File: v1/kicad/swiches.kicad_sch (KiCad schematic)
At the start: 13 parts, among them Q7 BC337

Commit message: Changed the file structure
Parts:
- SW1: value (none) -> SPST
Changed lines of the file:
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@@
 			)
 		)
-		(property "Value" ""
+		(property "Value" "SPST"
 			(at 64.77 55.88 0)
+			(hide yes)
 			(show_name no)
 			(do_not_autoplace no)
@@
 			)
 		)
-		(property "Description" "NPN transistor, collector/base/emitter"
+		(property "Description" ""
 			(at 88.9 55.88 0)
 			(hide yes)
@@
 			)
 		)
-		(property "Description" "Light emitting diode"
+		(property "Description" ""
 			(at 135.89 48.26 0)
 			(hide yes)
@@
 			)
 		)
-		(property "Description" "100V 0.15A standard switching diode, DO-35"
+		(property "Description" ""
 			(at 88.9 39.37 0)
 			(hide yes)
@@
 			)
 		)
-		(property "Description" "100V 0.15A standard switching diode, DO-35"
+		(property "Description" ""
 			(at 105.41 39.37 0)
 			(hide yes)
@@
 			)
 		)
-		(property "Description" "100V 0.15A standard switching diode, DO-35"
+		(property "Description" ""
 			(at 123.19 39.37 0)
 			(hide yes)
@@
 			)
 		)
-		(property "Description" "Light emitting diode"
+		(property "Description" ""
 			(at 140.97 48.26 0)
 			(hide yes)

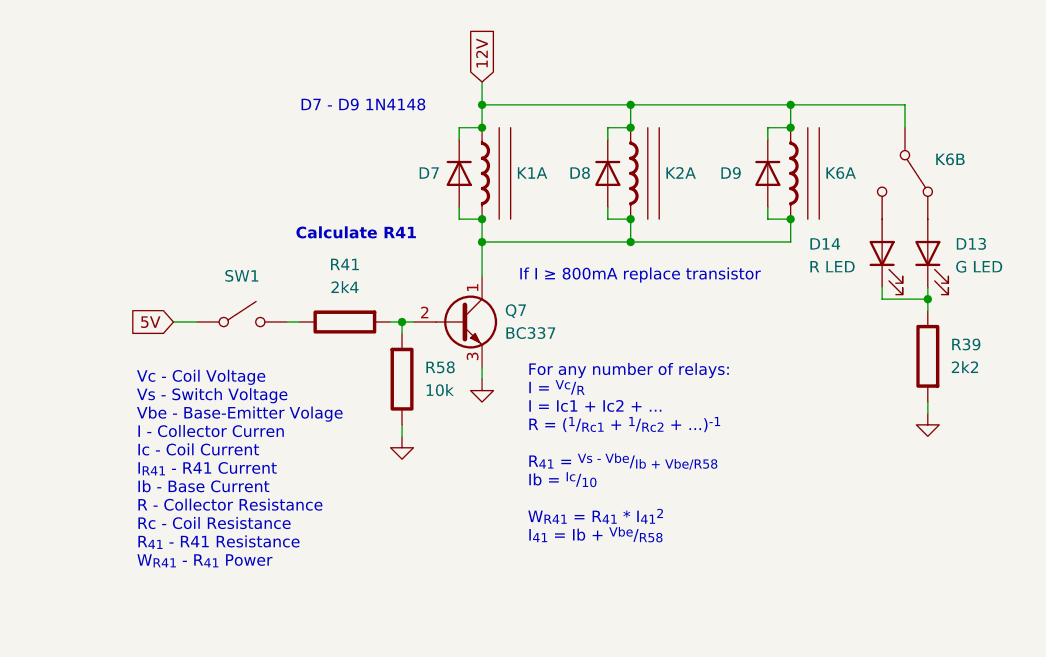
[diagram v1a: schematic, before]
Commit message: Added a DUT board, changed the output connectors , added test hooks, removed unnecessary switches, added FET support
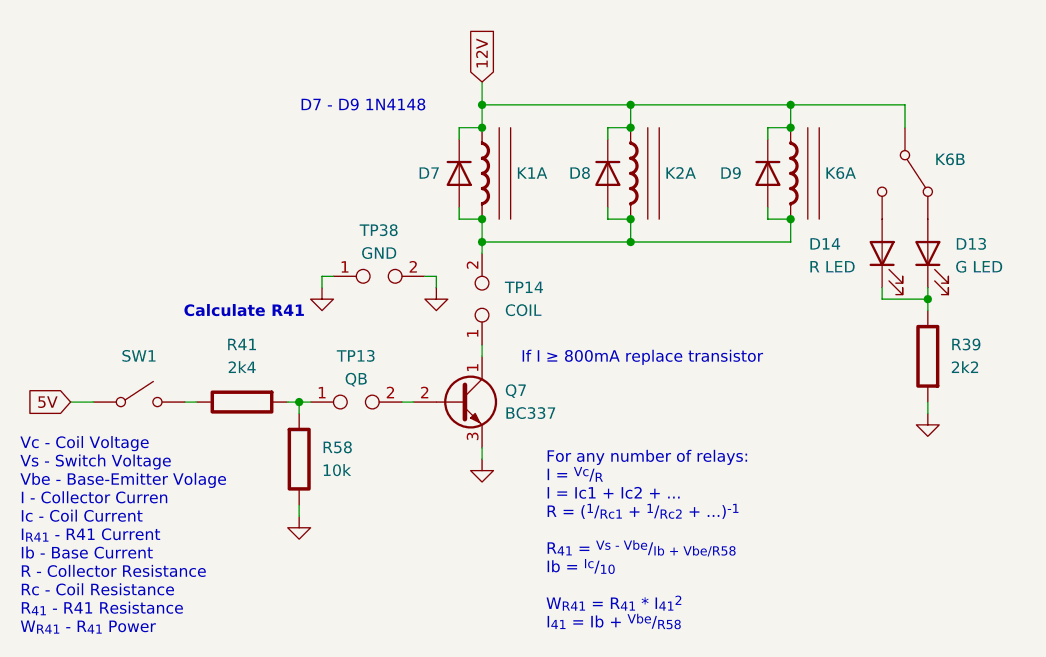
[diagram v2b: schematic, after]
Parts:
- added TP13: QB, symbol Connector:TestPoint_2Pole
- added TP14: COIL, symbol Connector:TestPoint_2Pole
- added TP38: GND, symbol Connector:TestPoint_2Pole
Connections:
- net GND: now also TP38.1, TP38.2
- new net: Q7.1 (C), TP14.1
- new net: Q7.2 (B), TP13.2
- new net: D7.2 (A), D8.2 (A), D9.2 (A), K1., K2., K6., TP14.2
- new net: R41., R58., TP13.1
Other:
- moved on the sheet: Q7, R41, R58, SW1

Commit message: Adding KiKit multiboarding
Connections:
- net GND renamed GNDD

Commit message: Fixed mistakes and made making a BOM easier
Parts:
- removed K6: (no value), symbol custom:Relay_Basic
- added K3: (no value), symbol custom:Relay-SPDT_Basic
- K1, K2, SW1: Spend (none) -> $$$
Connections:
- net 12V: now also K1.1, K2.1, K3.1, K3.3; no longer K1., K2.
- net 5V: now also SW1.1 (B); no longer SW1.2 (B)
- net GNDD: now also R39.1, R58.2; no longer R39., R58.
- net at D13.1 (K), D14.1 (K): now also R39.2; no longer R39.
- net at D14.2 (A): now also K3.5
- net at D13.2 (A): now also K3.4
- net at D7.2 (A), D8.2 (A), D9.2 (A)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: now also K1.2, K2.2, K3.2; no longer K1., K2.
- new net: R41.2, SW1.2 (A)
- new net: R41.1, R58.1, TP13.1
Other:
- note added: "N/P"
